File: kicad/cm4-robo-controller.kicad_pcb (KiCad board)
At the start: 2 copper layers, 145.8 x 76.9 mm, 49 parts, among them U1 ROBOCLAW-2X15A-OEM, U2 TPD4EUSB30DQAR-N, U3 FSUSB42MUX, U4 USB2514B-I/M2, U5 AP22653W6-7, U6 TPD4EUSB30DQAR-N, U7 TPD4EUSB30DQAR, U8 TPD4EUSB30DQAR, X1 X322524MOB4SI

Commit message: Ready to start layout
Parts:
- removed the C10 at (98.4, 112.8)
- removed the C7 at (92.5, 112.8)
- removed the C9 at (96.5, 112.8)
- removed the R17 at (143.9, 120.0)
- added A1: ROBOCLAW-2X15A-OEM, MyParts:MOD-TH_ROBOCLAW-OEM-2X15A, F.Cu at (175.1, 91.8)
- added BT1: ML414H-IV01E, MyParts:ML414H-IV01E, F.Cu at (-16.2, 104.9)
- added C1: 4.7nF, MyParts:C1206, F.Cu at (-60.1, 133.1)
- added C16: 100nF, MyParts:C0402, F.Cu at (17.2, 139.0)
- added C17: 100nF, MyParts:C0402, F.Cu at (17.2, 141.2)
- added C18: 100nF, MyParts:C0402, F.Cu at (17.2, 143.3)
- added C19: 100nF, MyParts:C0402, F.Cu at (17.2, 145.5)
- added C2: 100nF, MyParts:C0402, F.Cu at (32.5, 76.2)
- added C20: 100nF, MyParts:C0402, F.Cu at (17.2, 147.6)
- added C21: 100nF, MyParts:C0402, F.Cu at (17.2, 149.8)
- added C22: 10uF, MyParts:C0805, F.Cu at (29.3, 148.0)
- added C24: 100nF, MyParts:C0603, F.Cu at (-5.92, 117.5)
- added C25: 100nF, MyParts:C0603, F.Cu at (-5.92, 120.2)
- added C26: 10uF, MyParts:C1206, F.Cu at (8.12, 126.4)
- added C27: 100nF, MyParts:C0603, F.Cu at (-5.92, 122.8)
- added C28: 220uF, MyParts:CAP-SMD_BD6.3-L6.6-W6.6-FD, F.Cu at (14.7, 112.1)
- added C29: 100nF, MyParts:C0402, F.Cu at (-1.59, 127.9)
- added C30: 1uF, MyParts:C0603, F.Cu at (-5.92, 125.5)
- added C31: 100nF, MyParts:C0603, F.Cu at (-38.0, 102.7)
- added C32: 1uF, MyParts:C0603, F.Cu at (-38.0, 105.3)
- added C33: 10uF, MyParts:C0603, F.Cu at (-38.0, 108.0)
- added C34: 100nF, MyParts:C0603, F.Cu at (-38.0, 110.7)
- added C35: 100nF, MyParts:C0603, F.Cu at (-38.0, 113.4)
- added C36: 47pF, MyParts:C0603, F.Cu at (-38.0, 116.0)
- added C37: 10nF, MyParts:C0603, F.Cu at (-38.0, 118.7)
- added C38: 10uF, MyParts:C0805, F.Cu at (-12.9, 132.1)
- added C39: 100nF, MyParts:C0603, F.Cu at (-38.0, 121.4)
- added C40: 100nF, MyParts:C0402, F.Cu at (30.4, 102.4)
- added C41: 10uF, MyParts:C0805, F.Cu at (26.4, 102.8)
- added C42: 10uF, MyParts:C0805, F.Cu at (26.4, 105.8)
- added C43: 10uF, MyParts:C0805, F.Cu at (26.4, 108.7)
- added C44: 10uF, MyParts:C0805, F.Cu at (26.4, 111.7)
- added C45: 100uF, Capacitor_Tantalum_SMD:CP_EIA-7343-31_Kemet-D, F.Cu at (33.9, 115.0)
- added C46: DNP, MyParts:C0402, F.Cu at (30.4, 104.6)
- added C47: 100nF, MyParts:C0603, F.Cu at (40.8, 113.4)
- added C48: 10uF, MyParts:C0805, F.Cu at (26.4, 114.6)
- added C49: 10uF, MyParts:C0805, F.Cu at (26.4, 117.6)
- added C50: 10uF, MyParts:C0805, F.Cu at (26.4, 120.5)
- added C51: 10uF, MyParts:C0805, F.Cu at (26.4, 123.5)
- added C52: 10uF, MyParts:C0805, F.Cu at (26.4, 126.4)
- added C53: 10uF, MyParts:C0805, F.Cu at (26.4, 129.4)
- added C54: 100nF, MyParts:C0402, F.Cu at (30.4, 106.7)
- added C55: DNP, MyParts:C0402, F.Cu at (30.4, 108.9)
- added C56: 1.2nF, MyParts:C0402, F.Cu at (30.4, 111.0)
- added C57: 10nF, MyParts:C0402, F.Cu at (-27.7, 62.4)
- added C58: 10nF, MyParts:C0402, F.Cu at (-27.7, 64.5)
- added C59: 10nF, MyParts:C0402, F.Cu at (-27.7, 66.7)
- added C60: 10nF, MyParts:C0402, F.Cu at (-27.7, 68.8)
- added C61: 10nF, MyParts:C0402, F.Cu at (-27.7, 71.0)
- added C62: 100nF, MyParts:C0402, F.Cu at (-27.7, 73.1)
- added C63: 100nF, MyParts:C0402, F.Cu at (-27.7, 75.3)
- added CN1: SMA-KWE_C7498154, MyParts:SMA-TH_SMA-KWE_C7498154, F.Cu at (-23.7, 105.6)
- added D1: SMCJ18A_C53260906, MyParts:SMC_L6.9-W5.9-LS7.9-RD, F.Cu at (-47.6, 120.9)
- added D10: SMBJ18CA, PCM_JLCPCB:D_SMB, F.Cu at (15.8, 119.3)
- added D11: SMAJ20A, PCM_JLCPCB:D_SMA, F.Cu at (17.8, 103.6)
- added D12: 1N4148WS T4, MyParts:SOD-323_L1.8-W1.3-LS2.5-RD, F.Cu at (-28.8, 131.0)
- added D13: TPESD0402G12V, MyParts:D0402-BI, F.Cu at (-38.3, 126.1)
- added D14: BZT52C4V7, MyParts:SOD-123_L2.7-W1.6-LS3.7-RD, F.Cu at (-18.0, 132.1)
- added D15: SESD0402X1UN-0020-090, MyParts:DIO-SMD_2P-L1.0-W0.6-P0.65-RD, F.Cu at (-38.6, 128.2)
- added D16: TPESD0402G12V, MyParts:D0402-BI, F.Cu at (-27.4, 77.4)
- added D17: TPESD0402G12V, MyParts:D0402-BI, F.Cu at (-27.4, 79.6)
- added D18: TPESD0402G12V, MyParts:D0402-BI, F.Cu at (-27.4, 81.7)
- added D19: TPESD0402G12V, MyParts:D0402-BI, F.Cu at (-27.4, 83.9)
- added D2: BZT52C15, MyParts:SOD-123_L2.7-W1.6-LS3.7-RD, F.Cu at (-44.8, 133.2)
- added D20: TPESD0402G12V, MyParts:D0402-BI, F.Cu at (-27.4, 86.1)
- added D21: SMF6.0A, PCM_JLCPCB:D_SOD-123FL, F.Cu at (-51.1, 89.6)
- added D22: TPESD0402G12V, MyParts:D0402-BI, F.Cu at (-27.4, 88.2)
- added D23: SMF5.0A, PCM_JLCPCB:D_SOD-123FL, F.Cu at (-51.1, 92.9)
- added D24: SMF6.0A, PCM_JLCPCB:D_SOD-123FL, F.Cu at (-27.2, 146.8)
- added D3: SMCJ18A_C53260906, MyParts:SMC_L6.9-W5.9-LS7.9-RD, F.Cu at (-47.6, 128.1)
- added D4: BAT54S, MyParts:SOT-23-3_L2.9-W1.6-P1.90-LS2.8-BR, F.Cu at (33.4, 61.6)
- added D5: BAT54S, MyParts:SOT-23-3_L2.9-W1.6-P1.90-LS2.8-BR, F.Cu at (33.4, 65.8)
- added D6: BAT54C, MyParts:SOT-23-3_L2.9-W1.6-P1.90-LS2.8-BR, F.Cu at (24.4, 145.3)
- added D7: BAT54C, MyParts:SOT-23-3_L2.9-W1.6-P1.90-LS2.8-BR, F.Cu at (24.4, 149.5)
- added D9: SMF6.0A, PCM_JLCPCB:D_SOD-123FL, F.Cu at (29.5, 144.8)
- added F1: 15A, MyParts:FUSE-TH_4P-L19.8-W6.7_3557-2, F.Cu at (-59.7, 105.3)
- added F2: 5A, MyParts:FUSE-TH_4P-L19.8-W6.7_3557-2, F.Cu at (-59.7, 113.3)
- added F3: nSMD010, MyParts:F1206, F.Cu at (-45.4, 89.5)
- added FB1: 120Ω@100MHz, MyParts:L1206, F.Cu at (8.12, 129.7)
- added FB2: 120Ω@100MHz, MyParts:L0603, F.Cu at (-17.5, 116.9)
- added H1: M3, MountingHole:MountingHole_3.2mm_M3_Pad_Via, F.Cu at (-74.3, 105.3)
- added H2: M3, MountingHole:MountingHole_3.2mm_M3_Pad_Via, F.Cu at (-74.3, 113.3)
- added H3: M3, MountingHole:MountingHole_3.2mm_M3_Pad_Via, F.Cu at (-74.3, 121.2)
- added H4: M3, MountingHole:MountingHole_3.2mm_M3_Pad_Via, F.Cu at (-74.3, 129.2)
- added H5: 210S-1*2P L=11.6MMGold-plated black, MyParts:HDR-TH_2P-P2.54-V-M-1, F.Cu at (-66.2, 149.0)
- added H6: 210S-1*2P L=11.6MMGold-plated black, MyParts:HDR-TH_2P-P2.54-V-M-1, F.Cu at (-66.2, 152.8)
- added J1: KF7620-7.62-2P, MyParts:CONN-TH_P7.62_KF7620-7.62-2P, F.Cu at (-61.4, 123.3)
- added J10: KF2EDGR-2.54-2P, MyParts:CONN-TH_P2.54_KF2EDGR-2.54-2P, F.Cu at (-74.2, 89.7)
- added J11: KF7620-7.62-2P, MyParts:CONN-TH_P7.62_KF7620-7.62-2P, F.Cu at (-20.3, 39.1)
- added J12: KF2EDGR-2.54-2P, MyParts:CONN-TH_P2.54_KF2EDGR-2.54-2P, F.Cu at (-66.0, 89.7)
- added J13: KF2EDGR-2.54-2P, MyParts:CONN-TH_P2.54_KF2EDGR-2.54-2P, F.Cu at (-57.9, 89.7)
- added J14: KF7620-7.62-2P, MyParts:CONN-TH_P7.62_KF7620-7.62-2P, F.Cu at (-20.3, 53.2)
- added J2: HX PZ2.54-2X5P TP, MyParts:HDR-SMD_10P-P2.54-V-M-R2-C5-LS7.5, F.Cu at (29.4, 138.4)
- added J3: Header-Male-2.54_2x3, MyParts:HDR-TH_6P-P2.54-V-M-R2-C3-S2.54-1, F.Cu at (-73.8, 146.5)
- added J4: 2541WV-2X12P, MyParts:HDR-TH_24P-P2.54-V-M-R2-C12-S2.54, F.Cu at (-62.1, 140.2)
- added J5: Header-Male-2.54_1x3, MyParts:HDR-TH_3P-P2.54-V-M-1, F.Cu at (-65.0, 145.2)
- added J6: Header-Male-2.54_2x3, MyParts:HDR-TH_6P-P2.54-V-M-R2-C3-S2.54-1, F.Cu at (-73.8, 152.8)
- added J7: SMA-KWE_C7498154, MyParts:SMA-TH_SMA-KWE_C7498154, F.Cu at (-23.7, 114.2)
- added J8: KF2EDGR-2.54-4P, MyParts:CONN-TH_4P-P2.54_KF2EDGR-2.54-4P, F.Cu at (-19.6, 63.1)
- added J9: KF2EDGR-2.54-3P, MyParts:CONN-TH_3P-P2.54_KF2EDGR-2.54-3P, F.Cu at (-20.3, 78.2)
- added L1: 27nH, MyParts:L0402-RD, F.Cu at (-38.1, 123.8)
- added L2: 3.3uH, MyParts:IND-SMD_L7.3-W6.6_SRP7028A, F.Cu at (33.6, 122.0)
- added LED2: E6C0805UR, MyParts:LED0805-R-RD, F.Cu at (33.9, 69.5)
- added LED3: GREEN, MyParts:LED0805-R-RD, F.Cu at (14.4, 130.0)
- added LED4: XL-0805QBC, MyParts:LED0805-R-RD, F.Cu at (-16.6, 114.0)
- added NT1: NetTie, NetTie:NetTie-2_SMD_Pad2.0mm, F.Cu at (-66.8, 132.9)
- added Q1: SP40P04NK, MyParts:PDFN-8_L6.0-W5.0-P1.27_HGQ065NE4A, F.Cu at (-45.3, 105.2)
- added Q2: DMP6023LE-13, Package_TO_SOT_SMD:SOT-223-3_TabPin2, F.Cu at (4.86, 112.4)
- added Q3: NCE6008AS, MyParts:SOP-8_L4.9-W3.9-P1.27-LS6.0-BL, F.Cu at (8.45, 120.6)
- added Q4: BSS138, PCM_JLCPCB:Q_SOT-23, F.Cu at (-5.49, 129.2)
- added R11: 100kΩ, MyParts:R0603, F.Cu at (34.2, 144.4)
- added R18: 220Ω, MyParts:R0402, F.Cu at (12.2, 134.7)
- added R19: 220Ω, MyParts:R0402, F.Cu at (12.2, 136.9)
- added R20: 2.2kΩ, MyParts:R0402, F.Cu at (-59.1, 144.5)
- added R21: 2.2kΩ, MyParts:R0402, F.Cu at (-59.1, 146.6)
- added R22: 100kΩ, MyParts:R0603, F.Cu at (-5.96, 102.6)
- added R23: 3KΩ, MyParts:R0603, F.Cu at (-5.96, 105.0)
- added R24: 10kΩ, MyParts:R0603, F.Cu at (-5.96, 107.5)
- added R25: 10kΩ, MyParts:R0603, F.Cu at (-5.96, 110.0)
- added R26: 13kΩ, MyParts:R0603, F.Cu at (-5.96, 112.5)
- added R27: 180kΩ, MyParts:R0603, F.Cu at (-5.96, 114.9)
- added R28: 82kΩ, MyParts:R0603, F.Cu at (-2.04, 102.6)
- added R29: 330kΩ, MyParts:R0603, F.Cu at (-2.04, 105.0)
- added R30: 13kΩ, MyParts:R0603, F.Cu at (-2.04, 107.5)
- added R31: 10kΩ, MyParts:R0603, F.Cu at (-2.04, 110.0)
- added R32: 56kΩ, MyParts:R0603, F.Cu at (-2.04, 112.5)
- added R33: 100Ω, MyParts:R0402, F.Cu at (-22.1, 119.5)
- added R34: 1kΩ, MyParts:R0402, F.Cu at (-22.1, 121.6)
- added R35: 100Ω, MyParts:R0402, F.Cu at (-22.1, 123.8)
- added R36: 10kΩ, MyParts:R0603, F.Cu at (-12.0, 113.6)
- added R37: 100Ω, MyParts:R0402, F.Cu at (-22.1, 125.9)
- added R38: 100kΩ, MyParts:R0603, F.Cu at (-12.0, 116.0)
- added R39: 220Ω, MyParts:R0402, F.Cu at (-22.1, 128.1)
- added R40: 33Ω, MyParts:R2512, F.Cu at (-16.1, 128.1)
- added R41: 10Ω, MyParts:R1206, F.Cu at (31.8, 127.7)
- added R42: 12kΩ, MyParts:R0402, F.Cu at (39.8, 119.0)
- added R43: 20kΩ, MyParts:R0402, F.Cu at (39.8, 121.2)
- added R44: 2.2kΩ, MyParts:R0402, F.Cu at (39.8, 123.3)
- added R45: 100Ω, MyParts:R0402, F.Cu at (-24.2, 88.9)
- added R46: 100Ω, MyParts:R0402, F.Cu at (-24.2, 91.0)
- added R47: 5.1kΩ, MyParts:R0402, F.Cu at (-24.2, 93.2)
- added R48: 5.1kΩ, MyParts:R0402, F.Cu at (-24.2, 95.3)
- added R49: 100Ω, MyParts:R0402, F.Cu at (-24.2, 97.5)
- added R50: 100Ω, MyParts:R0402, F.Cu at (-21.1, 88.9)
- added R51: 5.1kΩ, MyParts:R0402, F.Cu at (-21.1, 91.0)
- added R52: 5.1kΩ, MyParts:R0402, F.Cu at (-21.1, 93.2)
- added R53: 100Ω, MyParts:R0402, F.Cu at (-21.1, 95.3)
- added R54: 100Ω, MyParts:R0402, F.Cu at (-21.1, 97.5)
- added R55: 5.1kΩ, MyParts:R0402, F.Cu at (-18.1, 88.9)
- added R56: 100Ω, MyParts:R0402, F.Cu at (-18.1, 91.0)
- added R57: 10kΩ, MyParts:R0402, F.Cu at (-18.1, 93.2)
- added R58: 15kΩ, MyParts:R0402, F.Cu at (-18.1, 95.3)
- added R59: 2.2kΩ, MyParts:R0402, F.Cu at (-38.5, 136.8)
- added R60: 10kΩ, MyParts:R0402, F.Cu at (-38.5, 139.0)
- added R61: 2.2kΩ, MyParts:R0402, F.Cu at (-38.5, 141.1)
- added R62: 5.1kΩ, MyParts:R0402, F.Cu at (-38.5, 143.3)
- added R63: 5.1kΩ, MyParts:R0402, F.Cu at (-38.5, 145.4)
- added SW1: SS-12F49-G050, MyParts:SW-TH_SS-12F45-GXXX, F.Cu at (6.83, 104.8)
- added TP1: TestPoint_Small, TestPoint:TestPoint_Pad_D1.5mm, F.Cu at (-47.4, 110.8)
- added TP10: TestPoint_Small, TestPoint:TestPoint_Pad_D1.5mm, F.Cu at (20.4, 142.5)
- added TP11: PWR_SW_G, MyParts:TESTPOINT-SMD_L3.0-W2.0, F.Cu at (2.46, 118.5)
- added TP12: 12V, MyParts:TESTPOINT-SMD_L3.0-W2.0, F.Cu at (2.46, 122.6)
- added TP13: VBAT, MyParts:TESTPOINT-SMD_L3.0-W2.0, F.Cu at (2.46, 126.6)
- added TP14: TestPoint_Small, TestPoint:TestPoint_Pad_D1.5mm, F.Cu at (-2.12, 117.9)
- added TP15: TestPoint_Small, TestPoint:TestPoint_Pad_D1.5mm, F.Cu at (-2.12, 121.5)
- added TP16: TestPoint_Small, TestPoint:TestPoint_Pad_D1.5mm, F.Cu at (-2.12, 125.0)
- added TP17: TestPoint_Small, TestPoint:TestPoint_Pad_D1.5mm, F.Cu at (-18.8, 120.2)
- added TP18: TestPoint_Small, TestPoint:TestPoint_Pad_D1.5mm, F.Cu at (-18.8, 123.7)
- added TP19: TestPoint_Small, TestPoint:TestPoint_Pad_D1.5mm, F.Cu at (-15.3, 120.2)
- added TP2: TestPoint_Small, TestPoint:TestPoint_Pad_D1.5mm, F.Cu at (-47.4, 114.4)
- added TP20: RH-5016, MyParts:TESTPOINT-SMD_L3.0-W2.0, F.Cu at (-33.5, 131.7)
- added TP21: TestPoint_Small, TestPoint:TestPoint_Pad_D1.5mm, F.Cu at (-15.3, 123.7)
- added TP22: TestPoint_Small, TestPoint:TestPoint_Pad_D1.5mm, F.Cu at (-11.7, 120.2)
- added TP23: TestPoint_Small, TestPoint:TestPoint_Pad_D1.5mm, F.Cu at (-11.7, 123.7)
- added TP24: 5V, MyParts:TESTPOINT-SMD_L3.0-W2.0, F.Cu at (40.8, 126.4)
- added TP25: TestPoint_Small, TestPoint:TestPoint_Pad_D1.5mm, F.Cu at (33.6, 103.1)
- added TP26: TestPoint_Small, TestPoint:TestPoint_Pad_D1.5mm, F.Cu at (33.6, 106.7)
- added TP27: TestPoint_Small, TestPoint:TestPoint_Pad_D1.5mm, F.Cu at (33.6, 110.2)
- added TP28: TestPoint_Small, TestPoint:TestPoint_Pad_D1.5mm, F.Cu at (-31.8, 146.9)
- added TP3: TestPoint_Small, TestPoint:TestPoint_Pad_D1.5mm, F.Cu at (32.9, 34.9)
- added TP4: TestPoint_Small, TestPoint:TestPoint_Pad_D1.5mm, F.Cu at (32.9, 38.4)
- added TP5: TestPoint_Small, TestPoint:TestPoint_Pad_D1.5mm, F.Cu at (32.9, 42.0)
- added TP6: TestPoint_Small, TestPoint:TestPoint_Pad_D1.5mm, F.Cu at (32.9, 45.5)
- added TP7: TestPoint_Small, TestPoint:TestPoint_Pad_D1.5mm, F.Cu at (32.9, 49.1)
- added TP8: TestPoint_Small, TestPoint:TestPoint_Pad_D1.5mm, F.Cu at (20.4, 135.4)
- added TP9: TestPoint_Small, TestPoint:TestPoint_Pad_D1.5mm, F.Cu at (20.4, 139.0)
- added U10: 74LVC1G07SE-7, MyParts:SC-88A_L2.0-W1.3-P0.65-LS2.1-BL, F.Cu at (-55.7, 145.3)
- added U11: MX26631DL, Package_DFN_QFN:QFN-24-1EP_4x4mm_P0.5mm_EP2.7x2.7mm_ThermalVias, F.Cu at (15.1, 125.2)
- added U12: MAX-M10S-00B, MyParts:SMD-18_L10.1-W9.7-P1.10-TL_SKG09F, F.Cu at (-29.8, 124.1)
- added U13: 74LVC1G17SE-7, MyParts:SC-88A_L2.0-W1.3-P0.65-LS2.1-BL, F.Cu at (-17.6, 110.4)
- added U14: 74LVC1G17SE-7, MyParts:SC-88A_L2.0-W1.3-P0.65-LS2.1-BL, F.Cu at (-14.1, 110.4)
- added U15: AP64501SP-13, MyParts:SOIC-8_L4.9-W3.9-P1.27-LS6.0-BL-EP-1, F.Cu at (38.6, 105.6)
- added U16: 74LVC1G17SE-7, MyParts:SC-88A_L2.0-W1.3-P0.65-LS2.1-BL, F.Cu at (-46.5, 93.2)
- added U17: 74LVC1G07SE-7, MyParts:SC-88A_L2.0-W1.3-P0.65-LS2.1-BL, F.Cu at (-35.1, 147.1)
- added U7: TPD4EUSB30DQAR, MyParts:USON-10_L2.5-W1.0-P0.50-BL, F.Cu at (33.7, 147.7)
- C10: renamed from C14; value 10uF 10V -> 10uF
- C11: renamed from C15; value 10uF 10V -> 10uF
- C12: renamed from C16; value 10uF 10V -> 10uF
- C13: renamed from C2; value 10uF 10V -> 10uF
- C14: renamed from C3; value 10uF 10V -> 10uF
- C15: renamed from C5; footprint PCM_JLCPCB:C_0402 -> MyParts:C0402
- C23: renamed from C17; footprint PCM_JLCPCB:C_0402 -> MyParts:C0402
- C3: renamed from C4; footprint PCM_JLCPCB:C_0402 -> MyParts:C0402
- C4: renamed from C1; footprint PCM_JLCPCB:C_0402 -> MyParts:C0402
- C5: renamed from C11; value 10uF 10V -> 10uF
- C6, C8: value 100n -> 100nF; footprint Capacitor_SMD:C_0402_1005Metric -> MyParts:C0402
- C7: renamed from C12; value 100uF 6.3V -> 100uF
- C9: renamed from C13; value 10uF 10V -> 10uF
- LED1: value RED -> GREEN
- Module1: footprint CM4_PARTS:Raspberry-Pi-4-Compute-Module -> MyParts:Raspberry-Pi-4-Compute-Module
- R1: value 10kΩ -> 47kΩ; footprint PCM_JLCPCB:R_0402 -> MyParts:R0402
- R12: renamed from R10; value 36K 1% -> 36kΩ
- R13: renamed from R11; value 36K 1% -> 36kΩ
- R14: renamed from R13; value 36K 1% -> 36kΩ
- R15: renamed from R14; value 36K 1% -> 36kΩ
- R16: value 1.5kΩ -> 10kΩ; footprint PCM_JLCPCB:R_0402 -> MyParts:R0402
- R17: renamed from R15; footprint PCM_JLCPCB:R_0402 -> MyParts:R0402
- R2: value 100Ω -> 1MΩ; footprint PCM_JLCPCB:R_0402 -> MyParts:R1206
- R3: renamed from R5; footprint PCM_JLCPCB:R_0402 -> MyParts:R0402
- R4: renamed from R3; footprint PCM_JLCPCB:R_0402 -> MyParts:R0402
- R5: renamed from R4; footprint PCM_JLCPCB:R_0402 -> MyParts:R0402
- R6, R8: value 2.2kΩ -> 10kΩ
- R7: value 5.1kΩ -> 10kΩ; footprint PCM_JLCPCB:R_0402 -> MyParts:R0402
- R9: value 5.1kΩ -> 1.5kΩ; footprint PCM_JLCPCB:R_0402 -> MyParts:R0402
- RJ1: value LPJG0926HENL_C22457393 -> HR911130A; footprint MyParts:RJ45-TH_LPJG0926HENL_C22457393 -> MyParts:RJ45-TH_HR911130A
- U1: value ROBOCLAW-2X15A-OEM -> 74LVC1G07SE-7; footprint MyParts:MOD-TH_ROBOCLAW-OEM-2X15A -> MyParts:SC-88A_L2.0-W1.3-P0.65-LS2.1-BL
- U5: renamed from U2; value TPD4EUSB30DQAR-N -> TPD4EUSB30DQAR; footprint MyParts:DFN-10_L2.5-W1.0-P0.50-BL-A -> MyParts:USON-10_L2.5-W1.0-P0.50-BL
- U6: value TPD4EUSB30DQAR-N -> TPD4EUSB30DQAR; footprint MyParts:DFN-10_L2.5-W1.0-P0.50-BL-A -> MyParts:USON-10_L2.5-W1.0-P0.50-BL
- X1: value X322524MOB4SI -> 24MHz
- moved R1 146.9 mm to (-55.5, 132.5), turned to 0 degrees
- moved U1 145.4 mm to (33.0, 73.2)
- moved USBC1 144.9 mm to (-31.6, 139.4), turned to 0 degrees
- moved R2 143.4 mm to (-50.2, 133.4), turned to 0 degrees
- moved RJ1 134.7 mm to (1.39, 147.2)
- moved R16 115.2 mm to (33.3, 150.5)
- moved R7 88.4 mm to (32.6, 54.1), turned to 0 degrees
- moved R6 88.4 mm to (32.6, 51.9), turned to 0 degrees
- moved R9 86.8 mm to (32.6, 58.4), turned to 0 degrees
- moved R8 86.7 mm to (32.6, 56.2), turned to 0 degrees
- moved C8 81.0 mm to (17.2, 136.9), turned to 0 degrees
- moved C6 76.6 mm to (17.2, 134.7), turned to 0 degrees
- moved Module1 37.6 mm to (125.1, 67.0), turned to 180 degrees
- moved R3 34.2 mm to (81.5, 178.6)
- moved U4 34.2 mm to (96.0, 170.2)
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- renumbered D1 to D8, R12 to R10, U3 to U2, U4 to U3, U5 to U4, U7 to U8, U8 to U9
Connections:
- net Net-(U3-HSD1+) renamed /CM4/usb/USB_HUB_P
- net Net-(U3-HSD1-) renamed /CM4/usb/USB_HUB_N
- C13 pad 2: 3V3_CM4 -> /3V3_CM4
- C14 pad 2: 3V3_CM4 -> /3V3_CM4
- C15 pad 1: 3V3_CM4 -> /3V3_CM4
- C23 pad 1: Net-(C17-Pad1) -> Net-(C23-Pad1)
- C5 pad 2: 5V -> /5V
- C6 pad 1: 3V3_CM4 -> /5V
- C8 pad 1: 3V3_CM4 -> /CM4/usb/VBUS
- LED1 pad 1: 5V -> /5V
- Module1 pad 15: /CM4/ETH_LEDY -> /CM4/ETH_LEDG
- Module1 pad 17: /CM4/ETH_LEDG -> /CM4/ETH_LEDY
- Module1 pad 24: unconnected-(Module1A-GPIO26-Pad24) -> /CM4/GPIO26
- Module1 pad 25: unconnected-(Module1A-GPIO21-Pad25) -> /CM4/GPIO21
- Module1 pad 26: unconnected-(Module1A-GPIO19-Pad26) -> /CM4/GPIO19
- Module1 pad 27: unconnected-(Module1A-GPIO20-Pad27) -> /CM4/GPIO20
- Module1 pad 28: /CM4/PWM1 -> /CM4/ROBO_RX_MCU
- Module1 pad 30: Net-(Module1A-GPIO6) -> /CM4/nPWR_CYCLE
- Module1 pad 31: /CM4/PWM0 -> /CM4/ROBO_TX_MCU
- Module1 pad 35: unconnected-(Module1A-ID_SC-Pad35) -> /CM4/GPIO1
- Module1 pad 36: unconnected-(Module1A-ID_SD-Pad36) -> /CM4/GPIO0
- Module1 pad 41: unconnected-(Module1A-GPIO25-Pad41) -> /CM4/PGOOD_12V
- Module1 pad 45: unconnected-(Module1A-GPIO24-Pad45) -> /CM4/~{FLT}
- Module1 pad 47: unconnected-(Module1A-GPIO23-Pad47) -> /CM4/GPIO23
- Module1 pad 48: unconnected-(Module1A-GPIO27-Pad48) -> /CM4/GPIO27
- Module1 pad 49: unconnected-(Module1A-GPIO18-Pad49) -> /CM4/GPIO18
- Module1 pad 50: unconnected-(Module1A-GPIO17-Pad50) -> /CM4/GPIO17
- Module1 pad 77: 5V -> /5V
- Module1 pad 78: 3V3_CM4 -> /3V3_CM4
- Module1 pad 79: 5V -> /5V
- Module1 pad 81: 5V -> /5V
- Module1 pad 83: 5V -> /5V
- Module1 pad 84: 3V3_CM4 -> /3V3_CM4
- Module1 pad 85: 5V -> /5V
- Module1 pad 86: 3V3_CM4 -> /3V3_CM4
- Module1 pad 87: 5V -> /5V
- Module1 pad 92: /CM4/RUN_PG -> unconnected-(Module1A-RUN_PG-Pad92)
- Module1 pad 94: /CM4/AIN1 -> /CM4/AIP1
- Module1 pad 96: /CM4/AIN0 -> /CM4/AIP0
- R1 pad 1: 3V3_CM4 -> Net-(D2-A)
- R1 pad 2: /CM4/MCU_nIRQ -> PGND
- R16 pad 1: /CM4/ETH_LEDG -> /CM4/usb/nOCS1
- R16 pad 2: Net-(R16-Pad2) -> /3V3_CM4
- R2 pad 1: /CM4/MCU_nIRQ -> CHASSIS
- R2 pad 2: Net-(Module1A-GPIO6) -> GND
- R4 pad 1: /CM4/CM4_TX -> /CM4/GPS_RX_MCU
- R5 pad 1: /CM4/CM4_RX -> /CM4/GPS_TX_MCU
- R6 pad 1: /CM4/USB_OTG_ID -> /CM4/AIN1
- R6 pad 2: GND -> /CM4/AIP1
- R7 pad 1: Net-(USBC1-CC1) -> /CM4/AIN0
- R7 pad 2: GND -> /CM4/AIP0
- R8 pad 1: /CM4/USB_OTG_ID -> /3V3_CM4
- R8 pad 2: Net-(R8-Pad2) -> /CM4/nPWR_LED
- R9 pad 1: Net-(USBC1-CC2) -> Net-(LED2-A)
- R9 pad 2: GND -> /5V
- RJ1 pad 11: unconnected-(RJ1-VC1-Pad11) -> /3V3_CM4
- RJ1 pad 12: unconnected-(RJ1-VC2-Pad12) -> Net-(R18-Pad1)
- RJ1 pad 13: unconnected-(RJ1-VC3-Pad13) -> Net-(R19-Pad2)
- RJ1 pad 14: unconnected-(RJ1-VC4-Pad14) -> /3V3_CM4
- U2 pad 1: 3V3_CM4 -> /3V3_CM4
- U3 pad 10: 3V3_CM4 -> /3V3_CM4
- U3 pad 15: 3V3_CM4 -> /3V3_CM4
- U3 pad 16: unconnected-(U4-PRTPWR2/BC_EN2-Pad16) -> /CM4/usb/PWR2
- U3 pad 18: unconnected-(U4-PRTPWR3/BC_EN3-Pad18) -> /CM4/usb/PWR3
- U3 pad 20: unconnected-(U4-PRTPWR4/BC_EN4-Pad20) -> /CM4/usb/PWR4
- U3 pad 23: 3V3_CM4 -> /3V3_CM4
- U3 pad 27: 3V3_CM4 -> /3V3_CM4
- U3 pad 29: 3V3_CM4 -> /3V3_CM4
- U3 pad 36: 3V3_CM4 -> /3V3_CM4
- U3 pad 5: 3V3_CM4 -> /3V3_CM4
- U3 pad 6: unconnected-(U4-USBDM_DN3/PRT_DIS_M3-Pad6) -> /CM4/usb/HD3_N
- U3 pad 7: unconnected-(U4-USBDP_DN3/PRT_DIS_P3-Pad7) -> /CM4/usb/HD3_P
- U3 pad 8: unconnected-(U4-USBDM_DN4/PRT_DIS_M4-Pad8) -> /CM4/usb/HD4_N
- U3 pad 9: unconnected-(U4-USBDP_DN4/PRT_DIS_P4-Pad9) -> /CM4/usb/HD4_P
- U4 pad 1: 5V -> /5V
- U4 pad 3: /CM4/usb/PWR1 -> /CM4/usb/U5_EN
- USB1 pad 9: GND -> CHASSIS
- USBC1 pad 1: GND -> CHASSIS
- USBC1 pad 2: GND -> CHASSIS
- USBC1 pad 3: GND -> CHASSIS
- USBC1 pad 4: GND -> CHASSIS
- USBC1 pad A4B9: Net-(R8-Pad2) -> Net-(D24-Pad1)
- USBC1 pad B4A9: Net-(R8-Pad2) -> Net-(D24-Pad1)

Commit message: Added new sheets, motor notes
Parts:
- removed TP5, TP6: TestPoint_Small, TestPoint:TestPoint_Pad_D1.5mm
- added J15: PM254-2-12-Z-8.5, MyParts:HDR-F-TH_2x12-P2.54-H8.5_PM254_NOPADS, F.Cu at (202.9, 77.7)
- added J16: PM254-2-09-Z-8.5, MyParts:HDR-F-TH_2x09-P2.54-H8.5_PM254_NOPADS, F.Cu at (164.2, 82.5)
- R57: value 10kΩ -> 68kΩ
- R58: value 15kΩ -> 100kΩ
- moved H2 285.4 mm to (205.0, 54.6)
- moved H3 279.6 mm to (205.0, 134.6)
- moved J13 257.8 mm to (196.7, 130.4)
- moved J12 256.6 mm to (187.3, 130.4)
- moved J10 255.4 mm to (178.0, 130.4)
- moved C61 229.8 mm to (192.0, 138.3), turned to -90 degrees
- moved F1 229.4 mm to (168.5, 128.6), turned to 90 degrees
- moved R1 229.2 mm to (173.6, 124.8), turned to -90 degrees
- moved Q1 224.7 mm to (178.9, 121.5), turned to -90 degrees
- moved D20 224.1 mm to (192.0, 131.7), turned to -90 degrees
- moved C60 221.6 mm to (182.7, 138.3), turned to -90 degrees
- moved NT1 220.9 mm to (154.1, 127.5), turned to 180 degrees
- moved D2 218.7 mm to (173.6, 121.2), turned to 90 degrees
- moved J1 215.8 mm to (154.3, 130.5)
- moved D19 215.5 mm to (182.7, 131.6), turned to -90 degrees
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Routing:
- net Net-(J1-Pad1): track 0.00 -> 1.02 mm
- added copper zone on In2.Cu, net /5V
- added copper zone on In2.Cu, net /V_MOTOR
- added copper zone on In1.Cu, net GND
- added copper zone on In1.Cu, net PGND
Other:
- board size 145.8 x 76.9 mm -> 150 x 90 mm
- copper layers 2 -> 4
- board text added: "+12.8V"
- board text added: "12.8VDC Battery"
- board text added: "2"
- board text added: "24"
- board text added: "AZ_LIMIT"
- board text added: "EL_LIMIT"
- board text added: "ESTOP"
- board text added: "GPIO"
- board text added: "Gnd"
- board text added: "USB2.0"

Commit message: Improved README
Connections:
- net /V_BAT renamed /battery-input/V_BAT
- net /V_MOTOR renamed /Robo/V_MOTOR
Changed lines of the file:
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@@
 			(size 3.2 2.2)
 			(layers "F.Cu" "F.Mask" "F.Paste")
-			(net "/V_BAT")
+			(net "/battery-input/V_BAT")
 			(pinfunction "1_1")
 			(pintype "passive")
@@
 			(layers "*.Cu" "*.Mask")
 			(remove_unused_layers no)
-			(net "/V_MOTOR")
+			(net "/Robo/V_MOTOR")
 			(pinfunction "1_1")
 			(pintype "passive")
@@
 			(layers "*.Cu" "*.Mask")
 			(remove_unused_layers no)
-			(net "/V_MOTOR")
+			(net "/Robo/V_MOTOR")
 			(pinfunction "2_2")
 			(pintype "passive")
@@
 			(layers "*.Cu" "*.Mask")
 			(remove_unused_layers no)
-			(net "/V_MOTOR")
+			(net "/Robo/V_MOTOR")
 			(pinfunction "BAT+_BAT+")
 			(pintype "power_in")
@@
 			(layers "*.Cu" "*.Mask")
 			(remove_unused_layers no)
-			(net "/V_MOTOR")
+			(net "/Robo/V_MOTOR")
 			(pinfunction "BAT+_BAT+")
 			(pintype "power_in")
@@
 			(layers "*.Cu" "*.Mask")
 			(remove_unused_layers no)
-			(net "/V_MOTOR")
+			(net "/Robo/V_MOTOR")
 			(pinfunction "BAT+_BAT+")
 			(pintype "power_in")
@@
 			(layers "*.Cu" "*.Mask")
 			(remove_unused_layers no)
-			(net "/V_MOTOR")
+			(net "/Robo/V_MOTOR")
 			(pinfunction "BAT+_BAT+")
 			(pintype "power_in")
@@
 			(size 1.5 1.5)
 			(layers "F.Cu" "F.Mask")
-			(net "/V_MOTOR")
+			(net "/Robo/V_MOTOR")
 			(pinfunction "1_1")
 			(pintype "passive")
@@
 			(size 1.485 1.728)
 			(layers "F.Cu" "F.Mask" "F.Paste")
-			(net "/V_BAT")
+			(net "/battery-input/V_BAT")
 			(pinfunction "1_1")
 			(pintype "passive")
@@
 			)
 		)
+		(property "ki_fp_filters" "D_*"
+			(at 0 0 90)
+			(unlocked yes)
+			(layer "F.Fab")
+			(hide yes)
+			(effects
+				(font
+					(size 1 1)
+					(thickness 0.15)
+				)
+			)
+		)
 		(property ki_fp_filters "D_*")
 		(sheetname "/CM4/usb/usb2/")
@@
 			(size 2.7 3.3)
 			(layers "F.Cu" "F.Mask" "F.Paste")
-			(net "/V_MOTOR")
+			(net "/Robo/V_MOTOR")
 			(pinfunction "C_1")
 			(pintype "passive")
@@
 			(size 2.7 3.3)
 			(layers "F.Cu" "F.Mask" "F.Paste")
-			(net "/V_BAT")
+			(net "/battery-input/V_BAT")
 			(pinfunction "C_1")
 			(pintype "passive")
@@
 			)
 		)
+		(property "ki_fp_filters" "D_*"
+			(at 0 0 90)
+			(unlocked yes)
+			(layer "F.Fab")
+			(hide yes)
+			(effects
+				(font
+					(size 1 1)
+					(thickness 0.15)
+				)
+			)
+		)
 		(property ki_fp_filters "D_*")
 		(sheetname "/Robo/")
@@
 			)
 		)
+		(property "ki_fp_filters" "D_*"
+			(at 0 0 0)
+			(unlocked yes)
+			(layer "F.Fab")
+			(hide yes)
+			(effects
+				(font
+					(size 1 1)
+					(thickness 0.15)
+				)
+			)
+		)
 		(property ki_fp_filters "D_*")
 		(sheetname "/Robo/")
@@
 			)
 		)
+		(property "ki_fp_filters" "D_*"
+			(at 0 0 0)
+			(unlocked yes)
+			(layer "F.Fab")
+			(hide yes)
+			(effects
+				(font
+					(size 1 1)
+					(thickness 0.15)
+				)
+			)
+		)
 		(property ki_fp_filters "D_*")
 		(sheetname "/CM4/usb/")
@@
 			(layers "*.Cu" "*.Mask")
 			(remove_unused_layers no)
-			(net "/V_BAT")
+			(net "/battery-input/V_BAT")
 			(pinfunction "1_1")
 			(pintype "passive")
@@
 			(layers "*.Cu" "*.Mask")
 			(remove_unused_layers no)
-			(net "/V_BAT")
+			(net "/battery-input/V_BAT")
 			(pinfunction "2_2")
 			(pintype "passive")
@@
 			)
 		)
+		(property "ki_fp_filters" "D_*"
+			(at 0 0 0)
+			(unlocked yes)
+			(layer "F.Fab")
+			(hide yes)
+			(effects
+				(font
+					(size 1 1)
+					(thickness 0.15)
+				)
+			)
+		)
 		(property ki_fp_filters "D_*")
 		(sheetname "/CM4/usb/")
@@
 	)
 	(zone
-		(net "/V_MOTOR")
+		(net "/Robo/V_MOTOR")
 		(layer "In2.Cu")
 		(name "VMOTOR_robo")

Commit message: Improved 3d image
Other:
- board text added: "Ethernet"
- board text added: "ROBOCLAW-2X15A-OEM"
- board text added: "Raspberry Pi Compute Module 4"
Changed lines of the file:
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@@
 			(at 18.38 -5.08 0)
 			(layer "F.SilkS")
+			(hide yes)
 			(effects
 				(font
@@
 		(layer "Edge.Cuts")
 	)
+	(gr_text "Ethernet"
+		(at 112.37 112.528709 0)
+		(layer "F.SilkS")
+		(effects
+			(font
+				(size 1 1)
+				(thickness 0.1)
+			)
+			(justify left bottom)
+		)
+	)
 	(gr_text "+12.8V"
 		(at 148.5 139.35 0)
@@
 	)
 	(gr_text "12.8VDC\nBattery"
-		(at 139.25 138.35 0)
+		(at 145.55 137.6 0)
 		(layer "F.SilkS")
 		(effects
@@
 				(thickness 0.15)
 			)
+			(justify right bottom)
+		)
+	)
+	(gr_text "Raspberry Pi Compute Module 4"
+		(at 80.25 91.1 0)
+		(layer "F.SilkS")
+		(effects
+			(font
+				(size 2 2)
+				(thickness 0.2)
+			)
+			(justify left bottom)
+		)
+	)
+	(gr_text "ROBOCLAW-2X15A-OEM"
+		(at 169.6 108.75 45)
+		(layer "F.SilkS")
+		(effects
+			(font
+				(size 2 2)
+				(thickness 0.2)
+			)
 			(justify left bottom)

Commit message: IPC footprint renaming, battery sim added
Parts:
- C1, C26: footprint MyParts:C1206 -> MyPartsIPC:CAPC3216X180N
- C10, C11, C12, C13, C14, C22, C38, C41, C42, C43, C44, C48, C49, C5, C50, C51, C52, C53, C9: footprint MyParts:C0805 -> MyPartsIPC:CAPC2012X145N
- C15, C16, C17, C18, C19, C2, C20, C21, C23, C29, C3, C4, C40, C54, C56, C57, C58, C59, C6, C60, C61, C62, C63, C8: footprint MyParts:C0402 -> MyPartsIPC:CAPC1005X55N
- C24, C25, C27, C30, C31, C32, C33, C34, C35, C36, C37, C39, C47: footprint MyParts:C0603 -> MyPartsIPC:CAPC1608X95N
- C28: footprint MyParts:CAP-SMD_BD6.3-L6.6-W6.6-FD -> MyPartsIPC:CAPAE660X770N
- C45, C7: footprint Capacitor_Tantalum_SMD:CP_EIA-7343-31_Kemet-D -> MyPartsIPC:CAPMP7343X310N
- C46: value DNP -> 470pF; footprint MyParts:C0402 -> MyPartsIPC:CAPC1005X55N
- C55: value DNP -> 33pF; footprint MyParts:C0402 -> MyPartsIPC:CAPC1005X55N
- D1, D3: footprint MyParts:SMC_L6.9-W5.9-LS7.9-RD -> MyPartsIPC:DIOM7959X262N
- D10: footprint PCM_JLCPCB:D_SMB -> MyPartsIPC:DIOM5436X244N
- D11: footprint PCM_JLCPCB:D_SMA -> MyPartsIPC:DIOM5226X244N
- D12: footprint MyParts:SOD-323_L1.8-W1.3-LS2.5-RD -> MyPartsIPC:SOD2513X110N
- D13, D16, D17, D18, D19, D20, D22: footprint MyParts:D0402-BI -> MyPartsIPC:DIOC1005X55N
- D14, D2: footprint MyParts:SOD-123_L2.7-W1.6-LS3.7-RD -> MyPartsIPC:SOD3716X135N
- D15: footprint MyParts:DIO-SMD_2P-L1.0-W0.6-P0.65-RD -> MyPartsIPC:DIOC1006X40N
- D21, D23, D24, D8, D9: footprint PCM_JLCPCB:D_SOD-123FL -> MyPartsIPC:SODFL3718X110N
- D4, D5, D6, D7: footprint MyParts:SOT-23-3_L2.9-W1.6-P1.90-LS2.8-BR -> MyPartsIPC:SOT95P280X110-3N
- F3: value nSMD010 -> 100mA; footprint MyParts:F1206 -> MyPartsIPC:FUSC3216X110N
- FB1: footprint MyParts:L1206 -> MyPartsIPC:INDC3216X130N
- FB2: footprint MyParts:L0603 -> MyPartsIPC:INDC1608X95N
- L1: footprint MyParts:L0402-RD -> MyPartsIPC:INDC1005X55N
- L2: footprint MyParts:IND-SMD_L7.3-W6.6_SRP7028A -> MyPartsIPC:INDM7366X280N
- LED1, LED2, LED3, LED4: footprint MyParts:LED0805-R-RD -> MyPartsIPC:LEDC2012X110N
- Q1: footprint MyParts:PDFN-8_L6.0-W5.0-P1.27_HGQ065NE4A -> MyPartsIPC:SON127P600X500X110-9N
- Q2: footprint Package_TO_SOT_SMD:SOT-223-3_TabPin2 -> MyPartsIPC:SOT230P700X180-4N
- Q3: footprint MyParts:SOP-8_L4.9-W3.9-P1.27-LS6.0-BL -> MyPartsIPC:SOIC127P600X175-8N
- Q4: footprint PCM_JLCPCB:Q_SOT-23 -> MyPartsIPC:SOT95P237X112-3N
- R1, R10, R12, R13, R14, R15, R16, R17, R18, R19, R20, R21, R3, R33, R34, R35, R37, R39, R4, R42, R43, R44, R45, R46, R47, R48, R49, R5, R50, R51, R52, R53, R54, R55, R56, R57, R58, R59, R6, R60, R61, R62, R63, R7, R8, R9: footprint MyParts:R0402 -> MyPartsIPC:RESC1005X40N
- R11, R22, R23, R24, R25, R26, R27, R28, R29, R30, R31, R32, R36, R38: footprint MyParts:R0603 -> MyPartsIPC:RESC1608X55N
- R2, R41: footprint MyParts:R1206 -> MyPartsIPC:RESC3216X70N
- R40: footprint MyParts:R2512 -> MyPartsIPC:RESC6332X70N
- U1, U10, U13, U14, U16, U17: footprint MyParts:SC-88A_L2.0-W1.3-P0.65-LS2.1-BL -> MyPartsIPC:SOT65P210X110-5N
- U11: footprint Package_DFN_QFN:QFN-24-1EP_4x4mm_P0.5mm_EP2.7x2.7mm_ThermalVias -> MyPartsIPC:QFN50P400X400X80-25N
- U15: footprint MyParts:SOIC-8_L4.9-W3.9-P1.27-LS6.0-BL-EP-1 -> MyPartsIPC:SOIC127P600X170-9N
- U2: footprint MyParts:MSOP-10_L3.0-W3.0-P0.50-LS5.0-BL -> MyPartsIPC:SOP50P500X110-10N
- U3: footprint MyParts:SQFN-36_L6.0-W6.0-P0.50-BL-EP -> MyPartsIPC:QFN50P600X600X100-37N
- U4: footprint MyParts:SOT-23-6_L2.9-W1.6-P0.95-LS2.8-BR -> MyPartsIPC:SOT95P280X145-6N
- U5, U6, U7, U8, U9: footprint MyParts:USON-10_L2.5-W1.0-P0.50-BL -> MyPartsIPC:SON50P100X250X60-10N

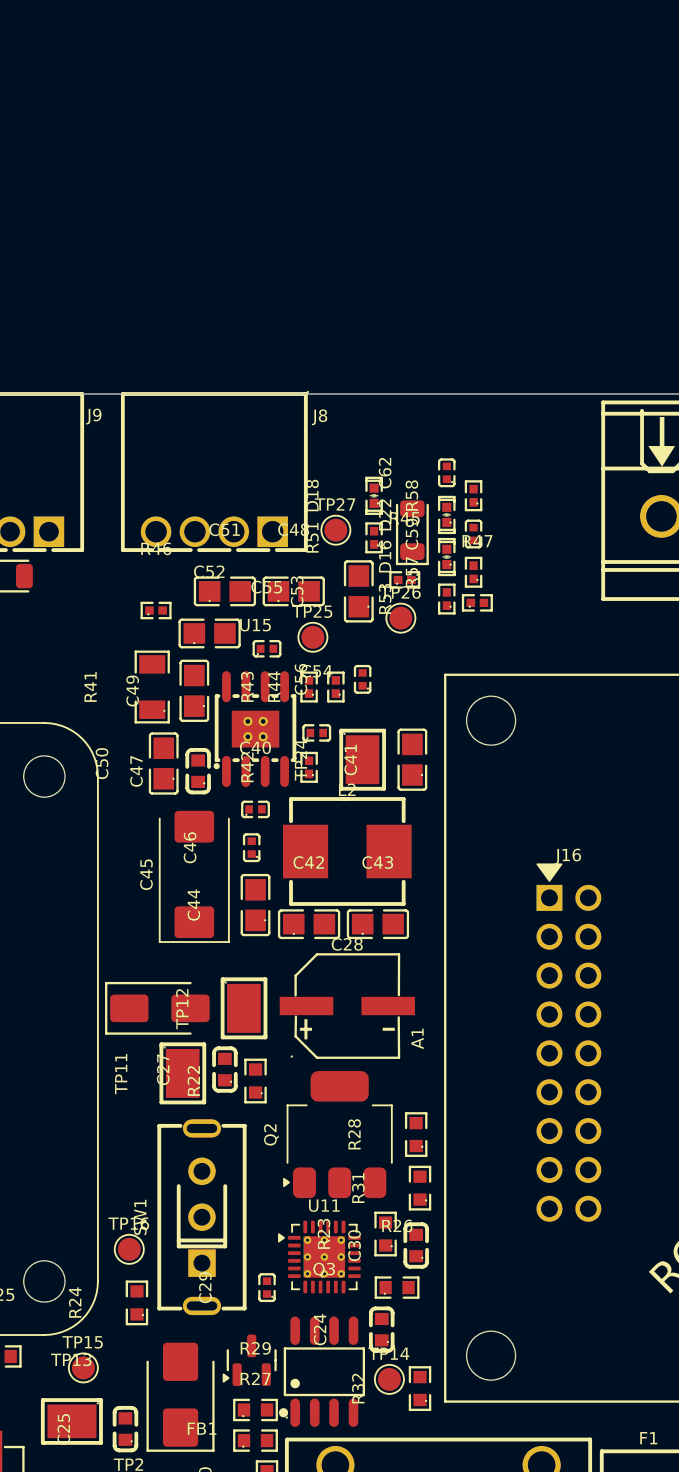
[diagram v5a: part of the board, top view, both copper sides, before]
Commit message: Updates after latest Tomachie review
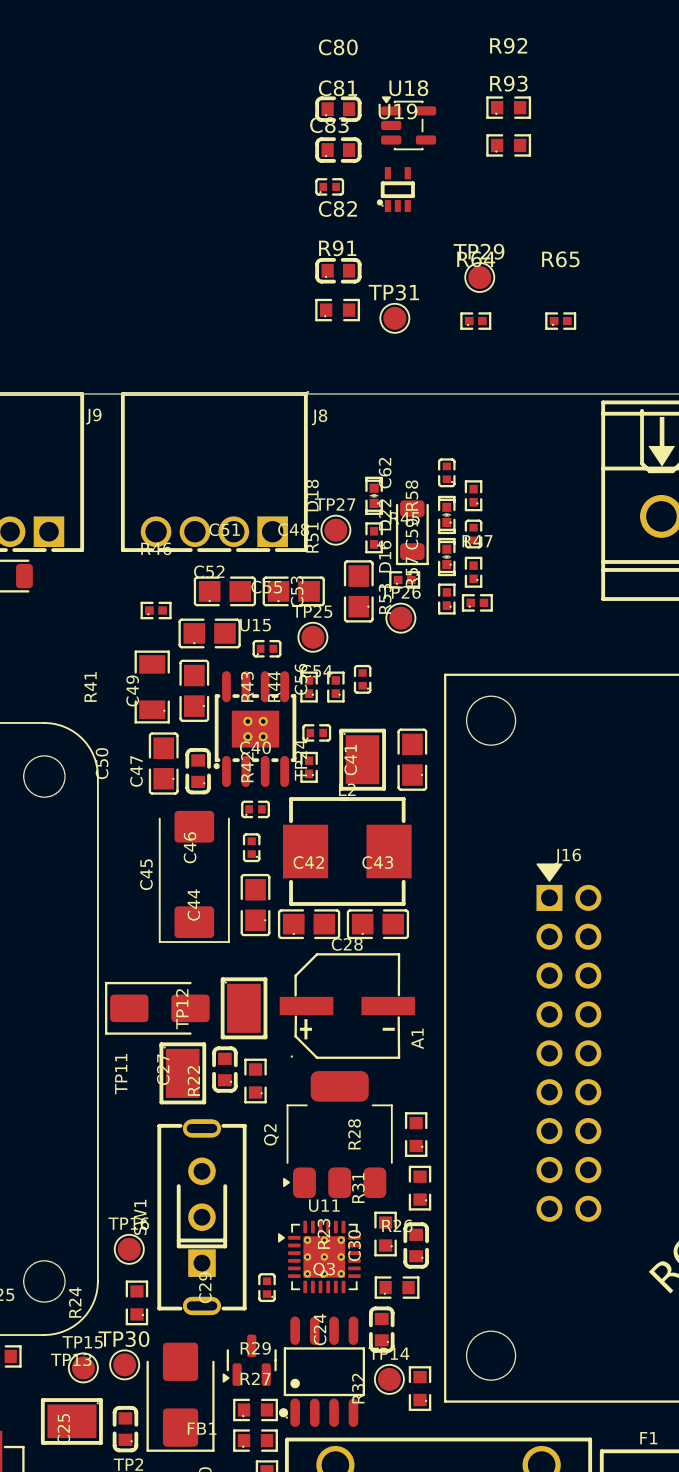
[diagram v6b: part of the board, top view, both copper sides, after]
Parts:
- added C80: 1uF, MyPartsIPC:CAPC1608X95N, F.Cu at (147.9, 31.0)
- added C81: 10uF, MyPartsIPC:CAPC1608X95N, F.Cu at (147.9, 33.7)
- added C82: 47nF, MyPartsIPC:CAPC1608X95N, F.Cu at (147.9, 41.5)
- added C83: 100nF, MyPartsIPC:CAPC1005X55N, F.Cu at (147.3, 36.1)
- added R64: 10kΩ, MyPartsIPC:RESC1005X40N, F.Cu at (156.9, 44.8)
- added R65: 100kΩ, MyPartsIPC:RESC1005X40N, F.Cu at (162.4, 44.8)
- added R91: 33kΩ, MyPartsIPC:RESC1608X55N, F.Cu at (147.9, 44.1)
- added R92: 330Ω, MyPartsIPC:RESC1608X55N, F.Cu at (159.0, 30.9)
- added R93: 10kΩ, MyPartsIPC:RESC1608X55N, F.Cu at (159.0, 33.4)
- added TP29: TestPoint_Small, TestPoint:TestPoint_Pad_D1.5mm, F.Cu at (157.2, 42.0)
- added TP30: TestPoint_Small, TestPoint:TestPoint_Pad_D1.5mm, F.Cu at (133.9, 113.0)
- added TP31: TestPoint_Small, TestPoint:TestPoint_Pad_D1.5mm, F.Cu at (151.6, 44.7)
- added U18: TPS70933DBVR, MyPartsIPC:SOT95P280X145-5N, F.Cu at (152.5, 32.0)
- added U19: 74LVC1G17SE-7, MyPartsIPC:SOT65P210X110-5N, F.Cu at (151.8, 36.2)
- R22: value 100kΩ -> 33kΩ
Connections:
- D12 pad 2: /3V3_CM4 -> Net-(D12-A)
- F3 pad 1: /3V3_CM4 -> Net-(U18-OUT)
- R46 pad 1: /CM4/ROBO_TX_MCU -> /Robo/ROBO_S1_RX
- SW1 pad 2: Net-(Q2-G) -> Net-(R91-Pad1)
- U15 pad 3: /power/12V -> /power/Power_5V/BUCK_EN
- U2 pad 10: GND -> /CM4/usb/MUX_OE
